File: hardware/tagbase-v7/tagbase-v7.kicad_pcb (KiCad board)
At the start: 2 copper layers, 50.8 x 69.9 mm, 40 parts, among them J1 Conn_01x04_Female, J101 Conn_02x03_Odd_Even, J102 Conn_02x05_Odd_Even, J104 USB_B_Mini, J2 Conn_01x06, J5 Conn_01x02, SW1 SW_DIP_x04, U1 XC6206, U105 Tactile Switch, U2 TS5A3159ADBVR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

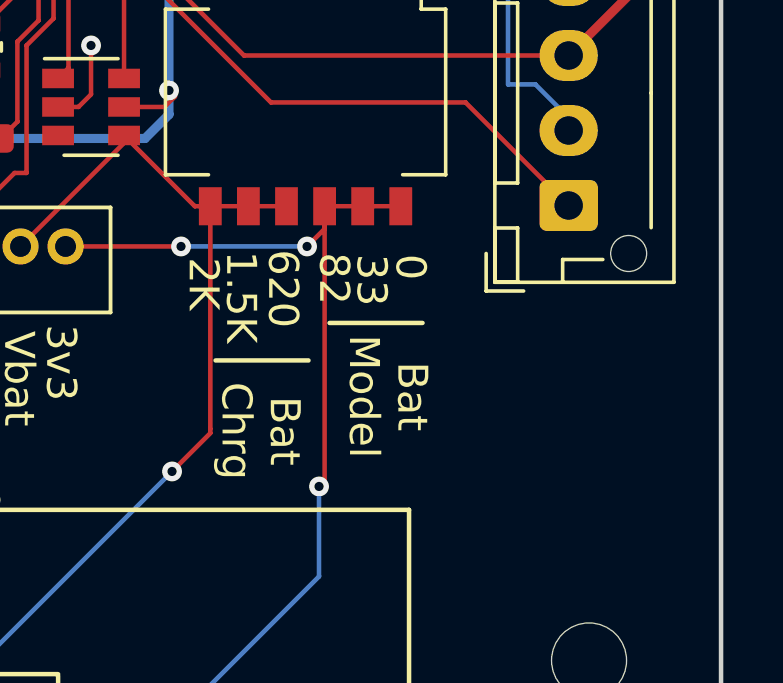
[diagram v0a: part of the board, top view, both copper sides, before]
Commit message: fix tagbase v7 for jlcpcb fabrication
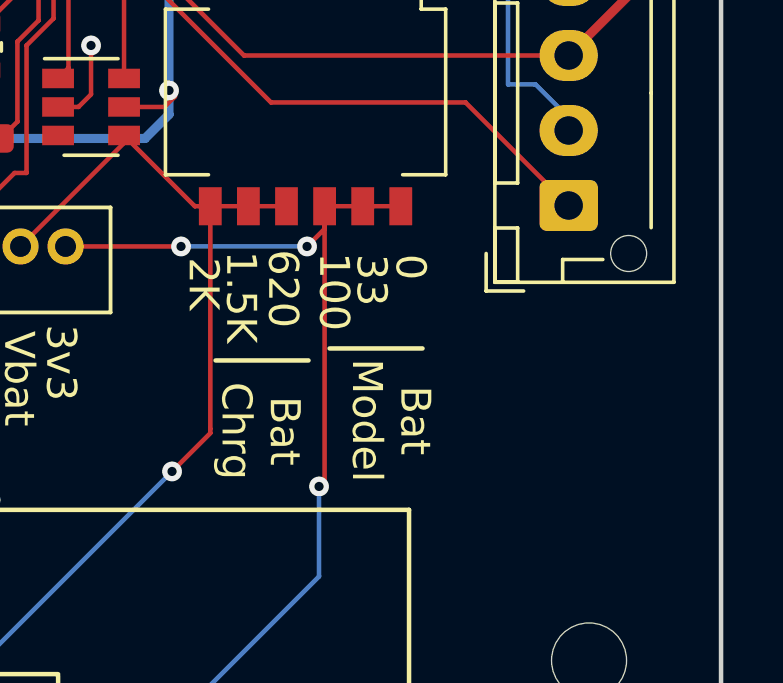
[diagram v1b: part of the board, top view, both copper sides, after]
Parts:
- R6: value 82 -> 100
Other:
- board text added: "100"
- board text removed: "82"
